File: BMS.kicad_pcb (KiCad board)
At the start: 2 copper layers, 86 x 86 mm, 115 parts, among them J1 Conn_01x06_Pin, J2 Conn_01x02_Pin, J5 Conn_01x02_Pin, J6 Conn_01x04_Pin, J7 USB_C_Receptacle_USB2.0_16P, Q1 MMFTP3401-AQ, Q3 SS8050, Q4 IRLZ44N, Q5 IRLZ44N, Q6 IRLZ44N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

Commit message: deklaracja warstw
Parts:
- U4: moved to F.Cu
- moved Q6 109.6 mm to (79.1, 84.8)
- moved D10 25.9 mm to (190.7, 66.0)
- moved D11 25.9 mm to (190.7, 71.5)
- moved D13 25.9 mm to (190.7, 77.1)
- moved C1 25.9 mm to (173.4, 64.7)
- moved C10 25.9 mm to (142.4, 87.2)
- moved C11 25.9 mm to (178.2, 64.7)
- moved C12 25.9 mm to (178.2, 67.7)
- moved C13 25.9 mm to (178.2, 70.7)
- moved C15 25.9 mm to (178.2, 73.7)
- moved C17 25.9 mm to (178.2, 76.8)
- moved C19 25.9 mm to (178.2, 79.8)
- moved C2 25.9 mm to (142.4, 66.6)
- moved C20 25.9 mm to (183.0, 64.7)
- moved C23 25.9 mm to (183.0, 67.7)
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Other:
- copper layers 2 -> 4

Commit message: pierwszy krok
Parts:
- U4: moved to B.Cu
- moved C11 133.7 mm to (47.5, 36.4)
- moved C12 132.8 mm to (47.6, 43.2)
- moved C13 132.1 mm to (47.7, 50.2)
- moved R23 131.7 mm to (45.7, 39.1), turned to 180 degrees
- moved R22 130.0 mm to (47.5, 34.2), turned to 180 degrees
- moved D2 129.3 mm to (88.5, 30.9), turned to 180 degrees
- moved D1 128.7 mm to (88.5, 28.9), turned to 180 degrees
- moved C20 124.6 mm to (59.0, 53.0)
- moved D7 120.3 mm to (65.9, 50.7)
- moved D13 101.8 mm to (99.7, 31.5), turned to 180 degrees
- moved U9 101.3 mm to (72.9, 53.0)
- moved R25 92.3 mm to (45.7, 46.0), turned to 180 degrees
- moved R21 90.9 mm to (45.6, 32.2), turned to 180 degrees
- moved R26 90.3 mm to (47.7, 48.1), turned to 180 degrees
- moved R24 90.2 mm to (47.7, 41.2), turned to 180 degrees
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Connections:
- C11 pad 1: /IO35 -> /IO36
- C12 pad 1: /IO36 -> /IO39
- C13 pad 1: /IO39 -> /IO34
- C20 pad 1: /IO34 -> /IO35
- D13 pad 2: /5V_USB -> +5V
- D7 pad 1: /IO34 -> /IO35
- R11 pad 1: /IO4 -> /IO17
- R14 pad 1: /IO17 -> /IO4
- R19 pad 1: /V3+ -> Net-(Q5-D)
- R19 pad 2: Net-(Q5-D) -> /V3+
- R21 pad 1: /IO35 -> /IO36
- R22 pad 2: /IO35 -> /IO36
- R23 pad 1: /IO36 -> /IO39
- R24 pad 2: /IO36 -> /IO39
- R25 pad 1: /IO39 -> /IO34
- R26 pad 2: /IO39 -> /IO34
- R42 pad 2: /IO34 -> /IO35
- U1 pad 5: /5V_USB -> +5V
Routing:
- net /CS: track 0.00 -> 57.9 mm
- net /SCK: track 0.00 -> 57.4 mm
- net /MOSI: track 0.00 -> 57.1 mm
- net /MISO: track 0.00 -> 56.9 mm
- net /EN: track 0.00 -> 52.4 mm, vias 0 -> 2
- net /V3+: track 0.00 -> 49.9 mm
- net /IO17: track 0.00 -> 49.3 mm
- net /V2+: track 0.00 -> 45.5 mm
- net /V1+: track 0.00 -> 41.1 mm
- net /IO16: track 0.00 -> 38.4 mm
- net /IO4: track 0.00 -> 27.4 mm
- net /IO34: track 0.00 -> 23.6 mm
- net /IO39: track 0.00 -> 21.2 mm
- net /TXD: track 0.00 -> 20.8 mm
- net /RXD: track 0.00 -> 20.7 mm
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
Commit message: update
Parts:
- C10, C3, D10, D11, L1, Q1, U11, U9: moved to B.Cu
- moved D11 173.7 mm to (18.0, 90.7), turned to 180 degrees
- moved D10 173.5 mm to (18.2, 84.0), turned to 180 degrees
- moved R44 130.4 mm to (59.6, 75.3), turned to 90 degrees
- moved TH1 129.7 mm to (51.3, 67.1)
- moved TH2 129.7 mm to (55.9, 67.1)
- moved R45 118.7 mm to (73.3, 84.2)
- moved C4 117.7 mm to (39.8, 22.7)
- moved D12 105.3 mm to (93.9, 94.8)
- moved R48 103.9 mm to (56.5, 92.9)
- moved R47 101.4 mm to (61.2, 92.8)
- moved C10 98.3 mm to (45.1, 73.4), turned to 180 degrees
- moved Q7 97.8 mm to (65.4, 95.1), turned to -90 degrees
- moved U13 92.8 mm to (58.3, 83.7), turned to -90 degrees
- moved C3 90.0 mm to (52.4, 75.7), turned to 180 degrees
- moved Q8 87.5 mm to (75.3, 95.0), turned to -90 degrees
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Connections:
- R11 pad 1: /IO17 -> /IO4
- R14 pad 1: /IO4 -> /IO17
- R19 pad 1: Net-(Q5-D) -> /V3+
- R19 pad 2: /V3+ -> Net-(Q5-D)
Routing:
- net /IO35: track 14.9 -> 0.00 mm
- net /V1+: track 41.1 -> 29.5 mm
- net /V2+: track 45.5 -> 36.7 mm
- net /IO36: track 19.1 -> 27.5 mm
- net /IO39: track 21.2 -> 28.4 mm
- net /IO17: track 49.3 -> 56.6 mm
- net /IO34: track 23.6 -> 29.0 mm
- net /IO16: track 38.4 -> 42.1 mm
- net /IO4: track 27.4 -> 24.9 mm
- net /V3+: track 49.9 -> 48.6 mm

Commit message: linki do TME
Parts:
- removed D9: MM3Zxx, Diode_SMD:D_SOD-323_HandSoldering
- added D8: D_Zener, Diode_SMD:D_SOD-323_HandSoldering, F.Cu at (127.4, 81.6)
- D12: footprint Diode_SMD:D_SMA_Handsoldering -> Diode_SMD:D_SMB_Handsoldering
- D7: value MM3Zxx -> D_Zener
- moved D7 58.0 mm to (127.4, 78.7)

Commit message: update
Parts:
- C2, C23, C25, C4, C5, C6, C7, C8, C9, D8, R3, R37, R47, R48, R5, R8, R9: moved to B.Cu
- U11, U9: moved to F.Cu
- moved D5 134.7 mm to (73.0, 50.6), turned to 180 degrees
- moved R34 134.1 mm to (49.9, 73.0), turned to 180 degrees
- moved R33 130.1 mm to (53.8, 68.7), turned to 90 degrees
- moved C25 129.4 mm to (55.7, 47.7), turned to 180 degrees
- moved C15 125.4 mm to (54.1, 91.7)
- moved C19 124.4 mm to (53.8, 76.9), turned to 180 degrees
- moved C5 122.9 mm to (56.1, 31.0), turned to -90 degrees
- moved C17 122.0 mm to (56.8, 64.8)
- moved D6 118.5 mm to (96.4, 44.6), turned to 90 degrees
- moved R36 102.0 mm to (46.6, 73.9), turned to -90 degrees
- moved R41 100.2 mm to (43.1, 63.3), turned to 90 degrees
- moved R3 99.5 mm to (45.3, 97.1), turned to 180 degrees
- moved C8 98.1 mm to (81.7, 41.9), turned to 90 degrees
- moved R29 96.9 mm to (50.6, 90.6), turned to 90 degrees
- moved R35 96.1 mm to (49.5, 60.3), turned to 180 degrees
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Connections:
- C19 pad 1: /IO32 -> /IO33
- C25 pad 1: /IO33 -> /IO32
- D8 pad 1: /IO33 -> /IO32
- R37 pad 2: /IO33 -> /IO32
- R39 pad 2: /IO32 -> /IO33
- R40 pad 1: /IO32 -> /IO33
- R43 pad 2: /IO26 -> /IO25
- R44 pad 2: /IO25 -> /IO26
- TH2 pad 1: /IO33 -> /IO32
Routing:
- net +5V: track 8.63 -> 177.8 mm, vias 2 -> 8
- net +3.3V: track 0.00 -> 147.2 mm, vias 0 -> 6
- net /V2+: track 36.7 -> 114.5 mm
- net /V1+: track 29.5 -> 100.4 mm
- net /V3+: track 48.6 -> 113.3 mm, vias 0 -> 1
- net Net-(Q5-D): track 0.00 -> 48.3 mm
- net Net-(Q4-D): track 0.00 -> 41.3 mm
- net /IO33: track 11.2 -> 52.2 mm
- net Net-(D10-K): track 0.00 -> 36.5 mm
- net /IO26: track 7.77 -> 40.7 mm
- net Net-(Q6-D): track 0.00 -> 30.6 mm
- net /IO25: track 9.61 -> 39.5 mm
- net +BATT: track 0.00 -> 25.4 mm
- net /V_out: track 0.00 -> 21.8 mm
- net Net-(R41-Pad2): track 0.00 -> 18.9 mm
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- added copper zone on F.Cu, net +BATT
- added copper zone on F.Cu, net /SENS_out
- added copper zone on F.Cu, net /V_out
- added copper zone on B.Cu, net GND
- added copper zone on F.Cu, net GND
- added copper zone on In1.Cu, net GND
- added copper zone on F.Cu, net Net-(Q7-D)

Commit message: update0.2
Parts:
- moved C5 4.06 mm to (60.1, 31.0), turned to 0 degrees
- moved C4 3.53 mm to (52.9, 30.9)
- moved R36 3.31 mm to (49.9, 74.6), turned to 180 degrees
- moved C2 2.75 mm to (62.9, 39.5), turned to -90 degrees
- moved R34 2.06 mm to (51.9, 72.5)
- moved C10 1.77 mm to (45.6, 84.6), turned to 0 degrees
- moved L1 1.32 mm to (31.7, 91.6)
- moved TH1 0.82 mm to (57.3, 67.6)
- moved R33 0.61 mm to (54.4, 68.7)
- moved C17 0.27 mm to (56.8, 64.5)
- moved D11 0.25 mm to (42.3, 91.6)
- moved R8 0.16 mm to (68.3, 50.7)
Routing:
- net +3.3V: track 147.2 -> 137.0 mm, vias 6 -> 7
- net +5V: track 177.8 -> 185.4 mm
- net Net-(U9A--): track 4.08 -> 5.23 mm
- net Net-(D11-K): track 11.1 -> 12.1 mm
- net /V_temp: track 5.55 -> 6.48 mm
- net Net-(U9C-+): track 12.0 -> 12.6 mm
- net GND: vias 183 -> 186
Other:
- board text added: "+3.3V"
- board text added: "BOOT"
- board text added: "CLK"
- board text added: "CS"
- board text added: "EN"
- board text added: "GND"
- board text added: "IN +12V"
- board text added: "MISO"
- board text added: "MOSI"
- board text added: "OUT +12V"
- board text added: "SPI"
- board text added: "V1+"
- board text added: "V2+"
- board text added: "V3+"

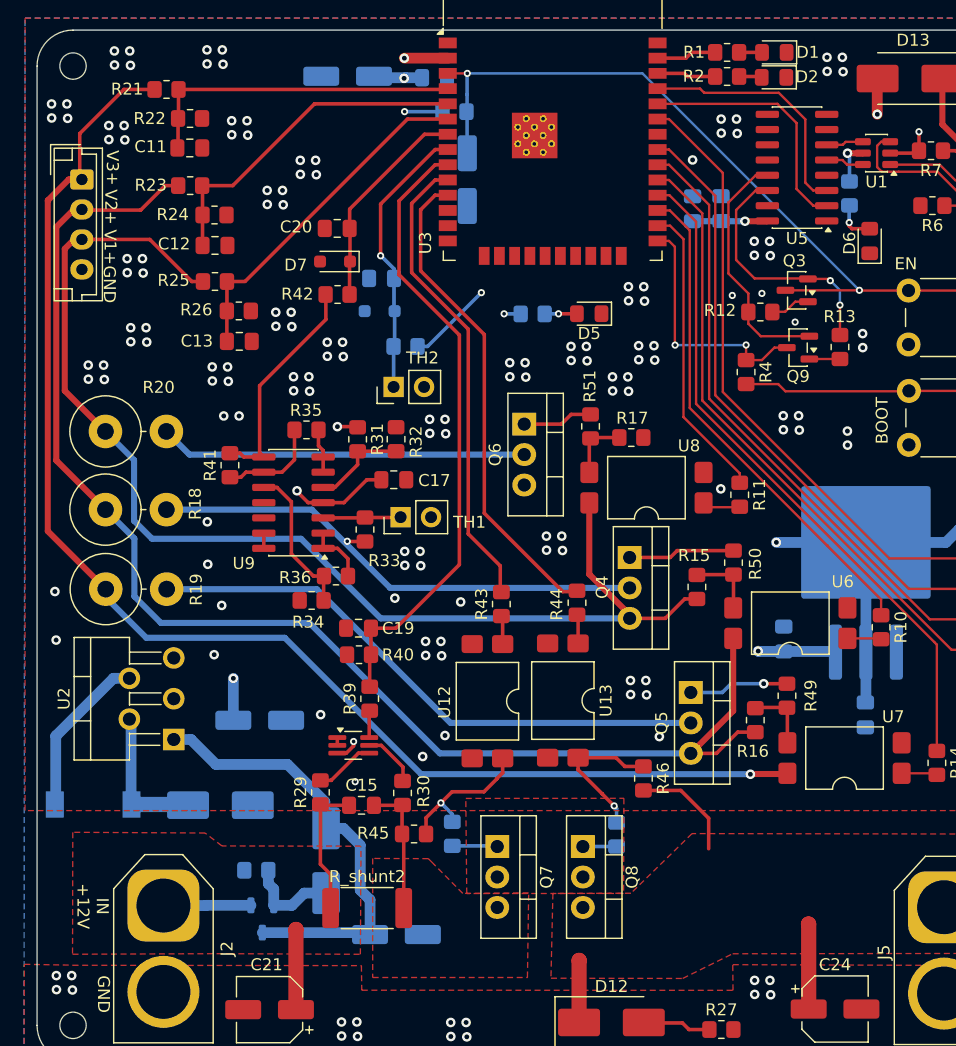
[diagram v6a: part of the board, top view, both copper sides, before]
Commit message: rezystory po 100 ohm do pt100
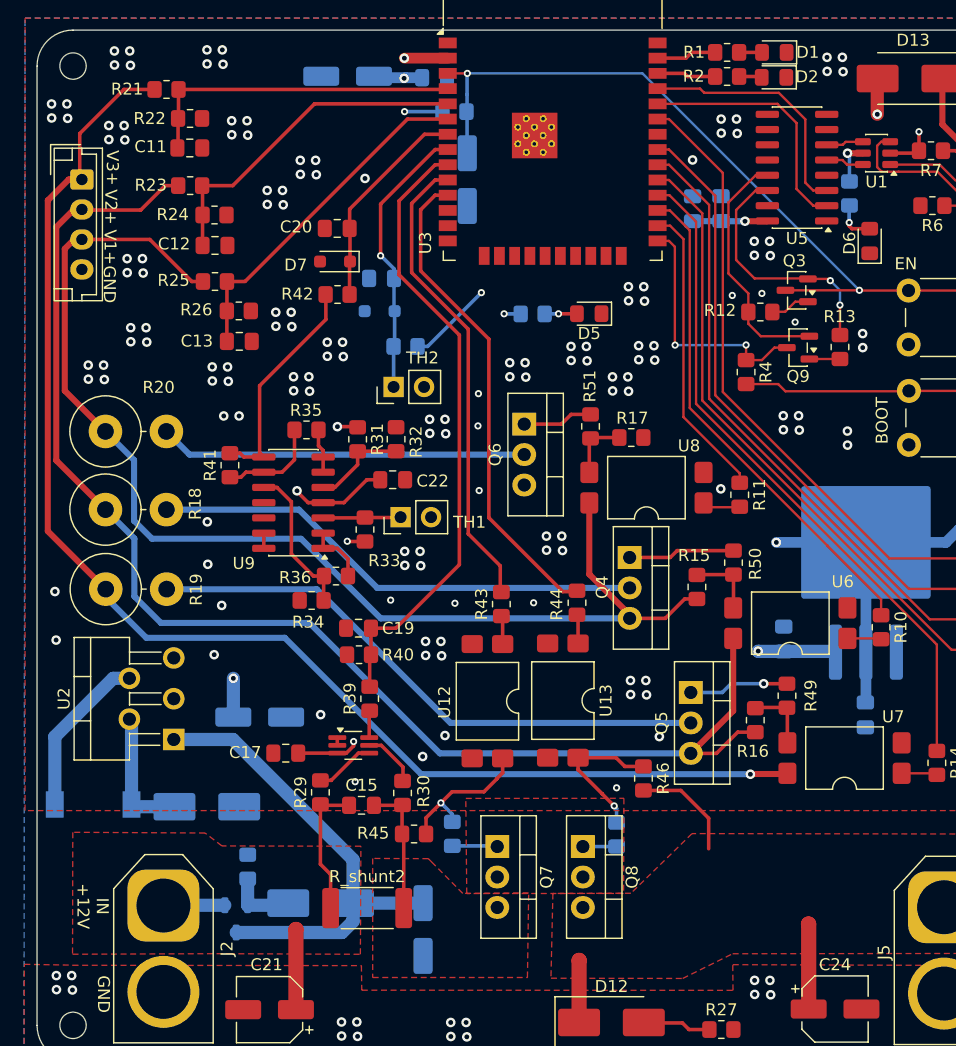
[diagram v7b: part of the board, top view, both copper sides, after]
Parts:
- added C22: 100n, Capacitor_SMD:C_0805_2012Metric_Pad1.18x1.45mm_HandSolder, F.Cu at (56.7, 64.5)
- R31, R33: value 2.2k -> 100
- moved C17 24.5 mm to (47.7, 87.3), turned to 180 degrees
- moved D10 3.57 mm to (50.6, 99.8), turned to 180 degrees
- moved C3 2.26 mm to (59.2, 102.0), turned to -90 degrees
- moved Q1 2.18 mm to (43.6, 101.1)
- moved D11 1.14 mm to (41.2, 91.8)
- moved R3 0.78 mm to (44.6, 96.8), turned to 90 degrees
- moved C10 0.27 mm to (45.6, 84.3)
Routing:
- net Net-(D10-K): track 36.5 -> 40.2 mm
- net Net-(D10-A): track 7.89 -> 5.68 mm
- net +BATT: track 25.4 -> 23.3 mm
- net Net-(D11-K): track 12.1 -> 11.1 mm
- net +5V: track 185.4 -> 184.4 mm
- net GND: vias 186 -> 192
- added copper zone on In2.Cu, net GND
